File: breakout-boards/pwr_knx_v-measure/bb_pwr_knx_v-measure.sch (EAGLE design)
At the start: 47 parts, among them IC100 BD9G101, T1 BC856, T2 BCP52, T3 BC847

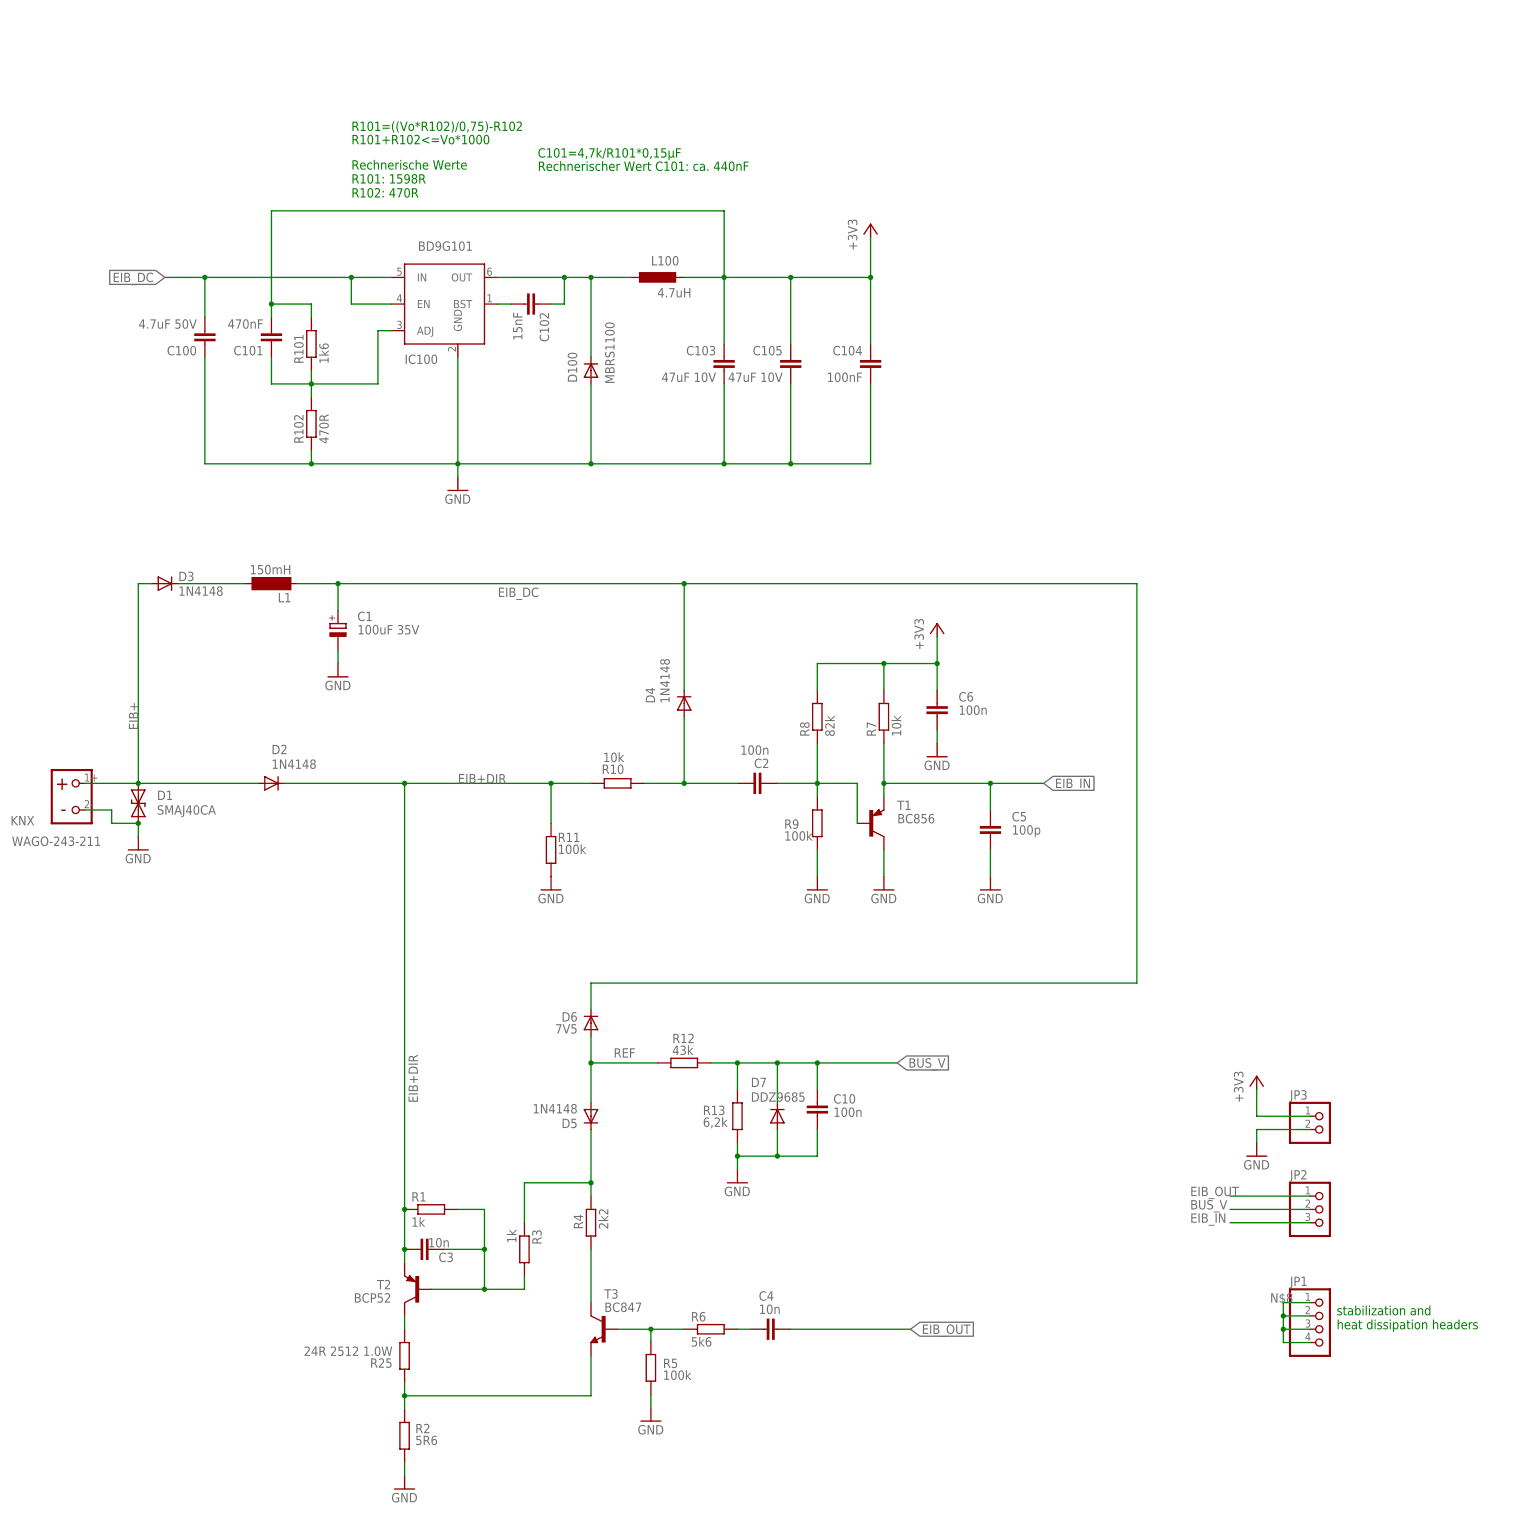
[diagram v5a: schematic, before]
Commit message: [BB_Pwr+KNX] - rearranged parts, reduced heat dissipation pins to 2
rearrangement in order to avoid by accident wrongly placed parts and connected pin headers
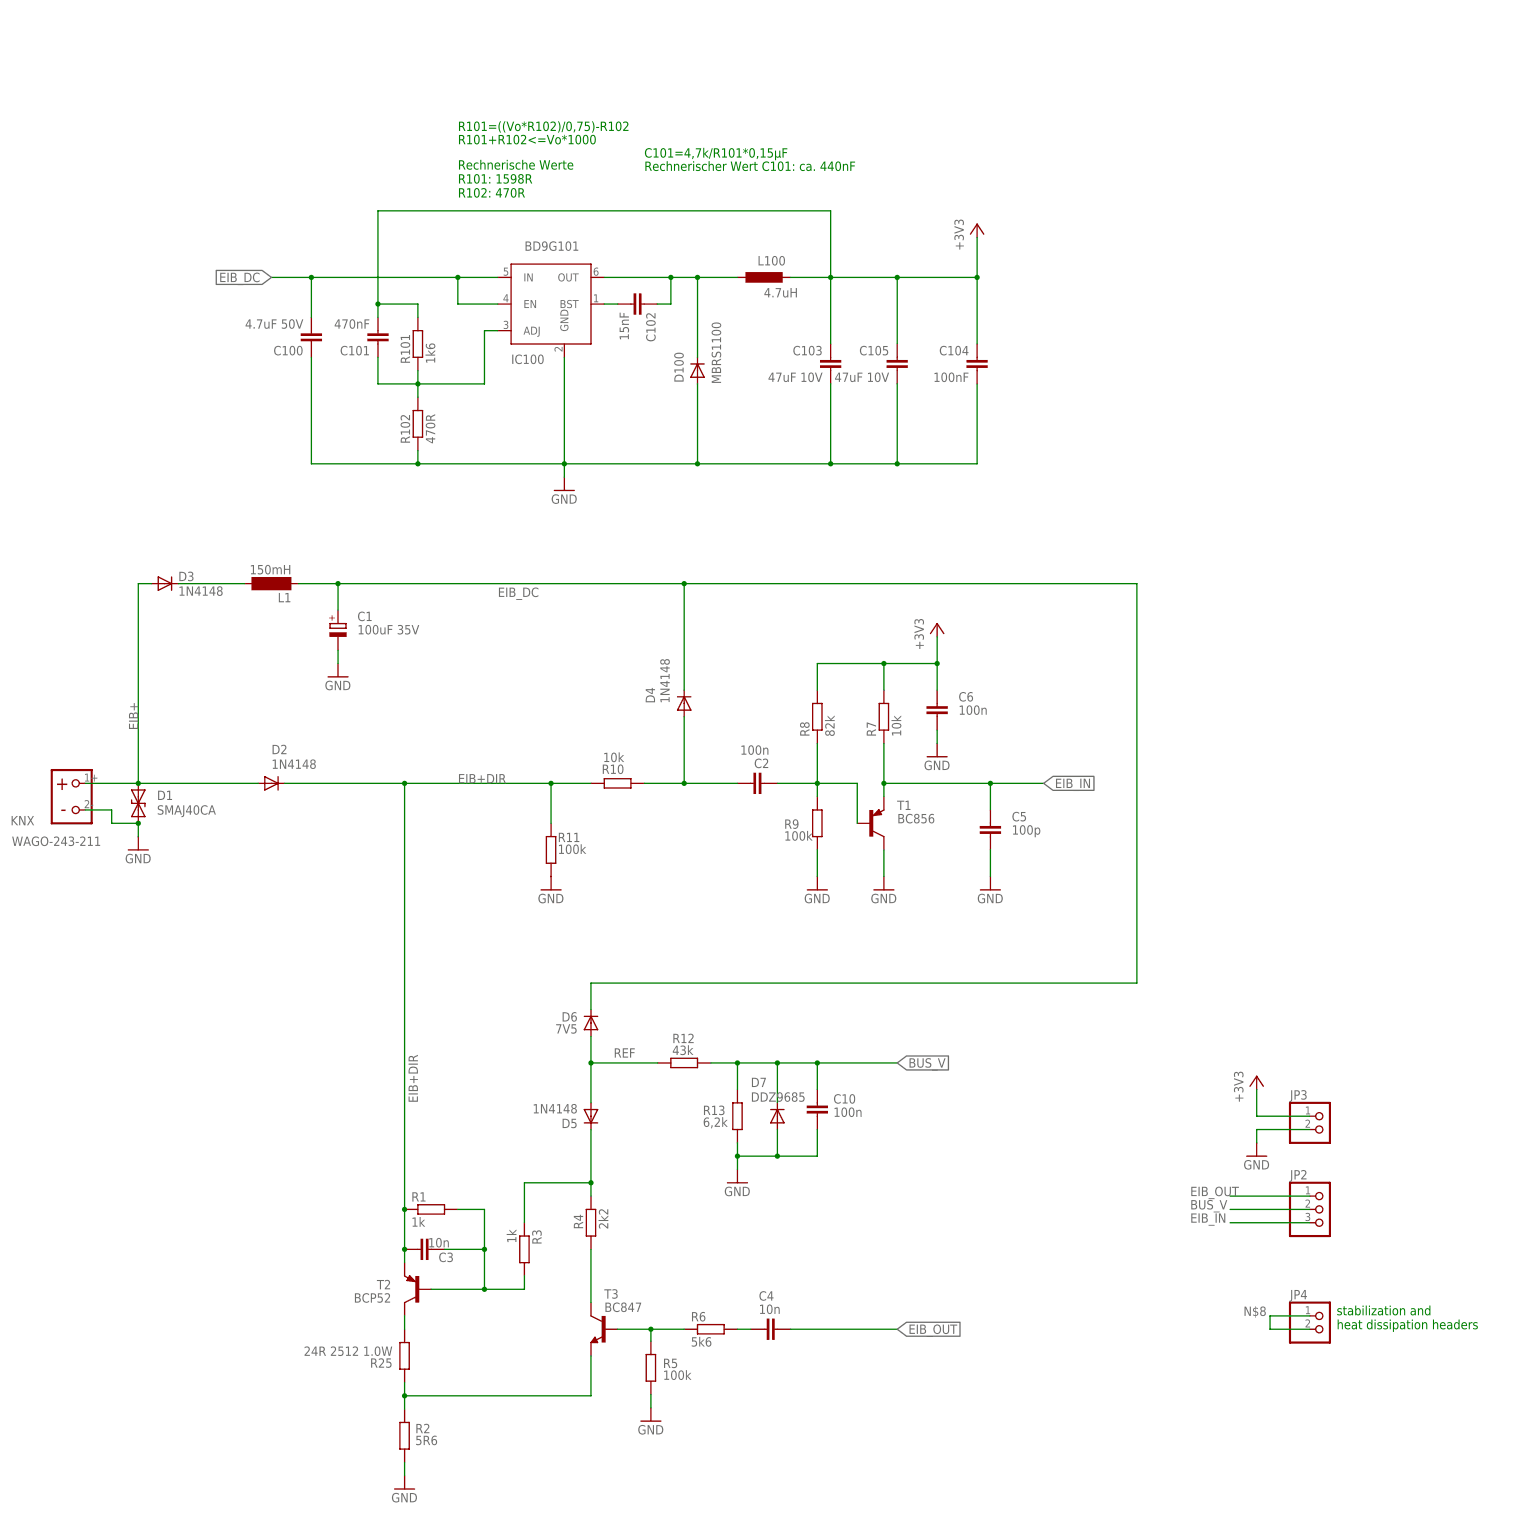
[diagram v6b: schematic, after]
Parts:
- removed JP1: (no value), pinhead_dmx:PINHD-1X4
- added JP4: (no value), pinhead_dmx:PINHD-1X2
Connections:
- net N$8: now also JP4.1, JP4.2; no longer JP1.1, JP1.2, JP1.3, JP1.4
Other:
- moved on the sheet: C100, C101, C102, C103, C104, C105, D100, IC100, L100, R101, R102

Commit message: [BB_Pwr+KNX] - labels rearranged; MLCC values updated
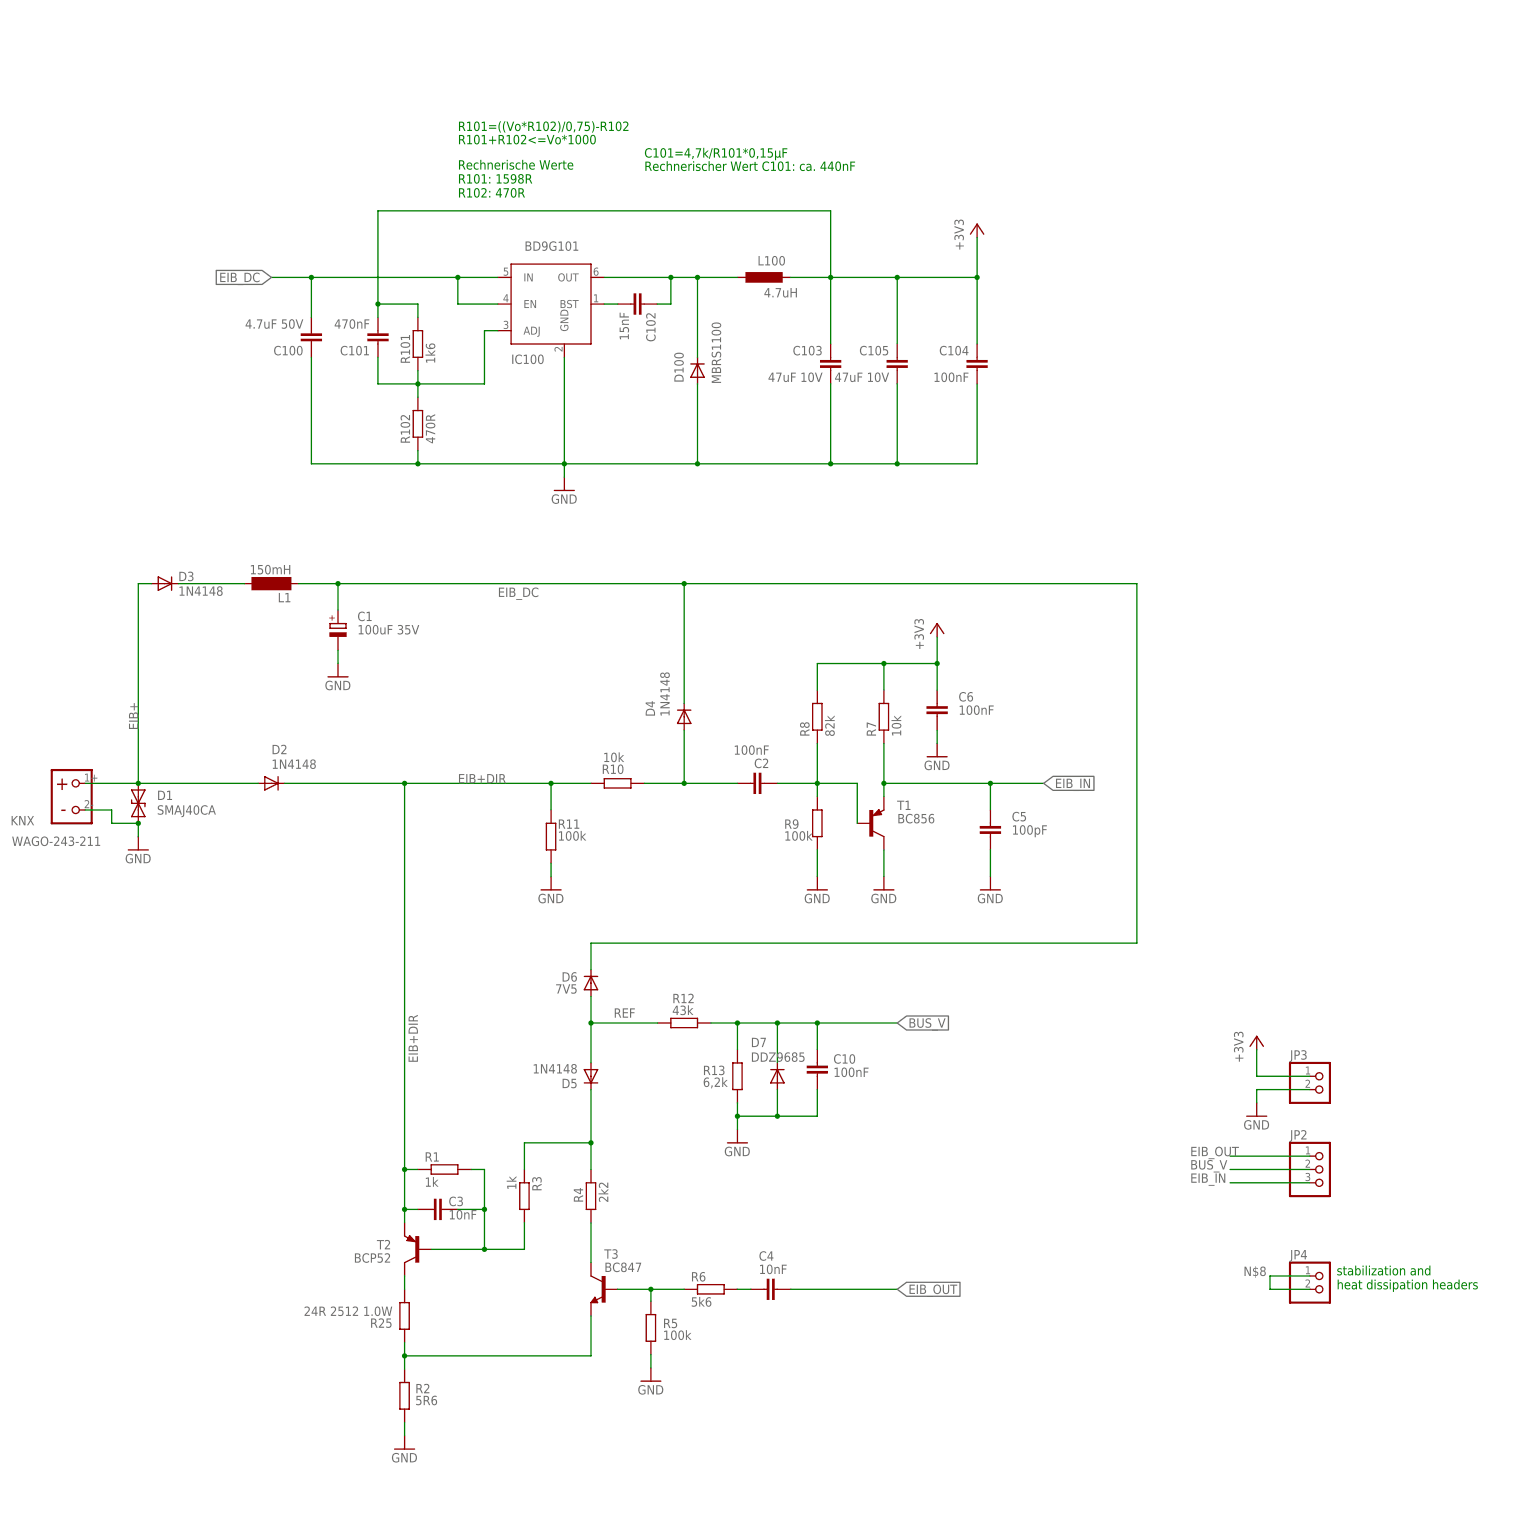
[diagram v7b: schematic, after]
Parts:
- C10, C2, C6: value 100n -> 100nF
- C3, C4: value 10n -> 10nF
- C5: value 100p -> 100pF
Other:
- moved on the sheet: C10, C3, C4, D4, D5, D6, D7, JP2, JP3, JP4, R1, R11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
